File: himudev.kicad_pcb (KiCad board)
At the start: 4 copper layers, 93.6 x 43.6 mm, 132 parts, among them J1 USB_C16PIN, J2 M20-8770642R, J3 M20-8770642R, J4 20021121-00010C4LF, J5 M20-8762042, Q1 IRLML6402, Q2 BSS214NW, Q3 BSS214NW, Q4 BSS214NW, Q5 BSS214NW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

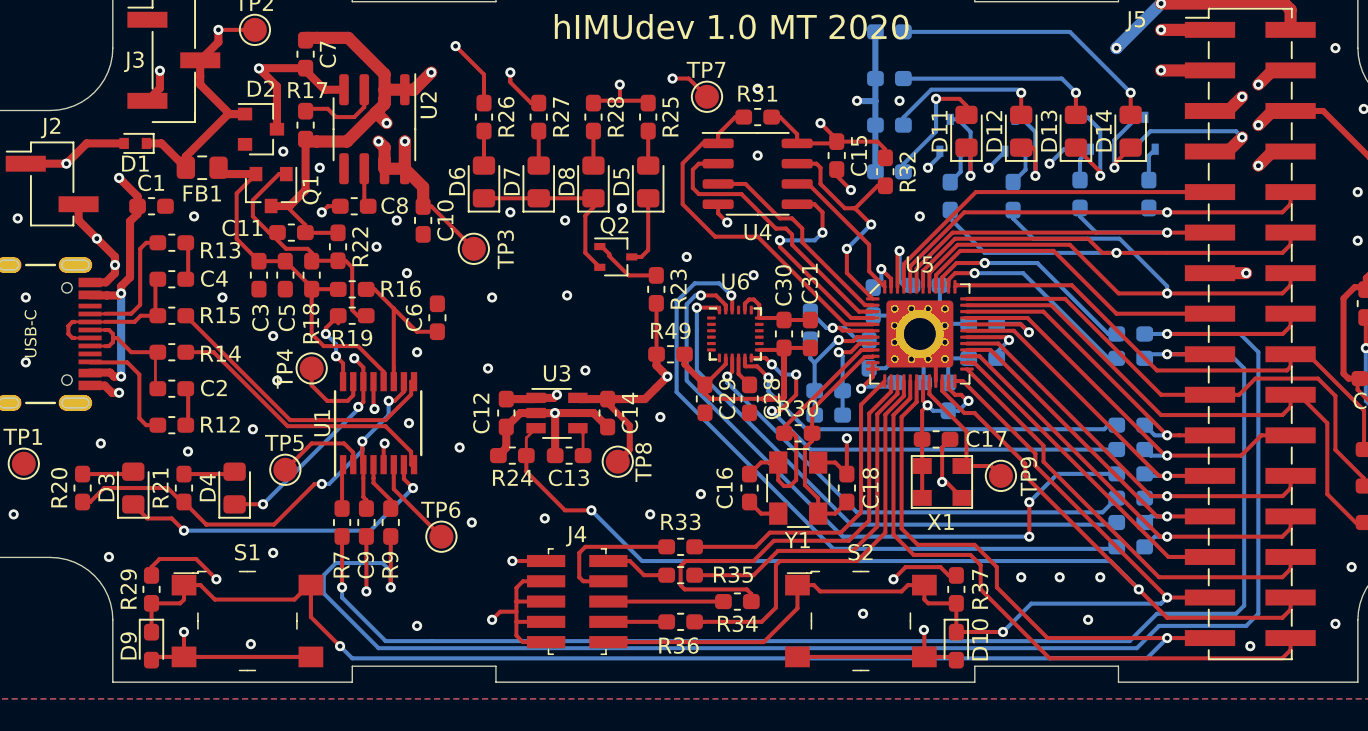
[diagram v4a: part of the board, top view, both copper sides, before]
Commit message: Small via & silkscreen fixes
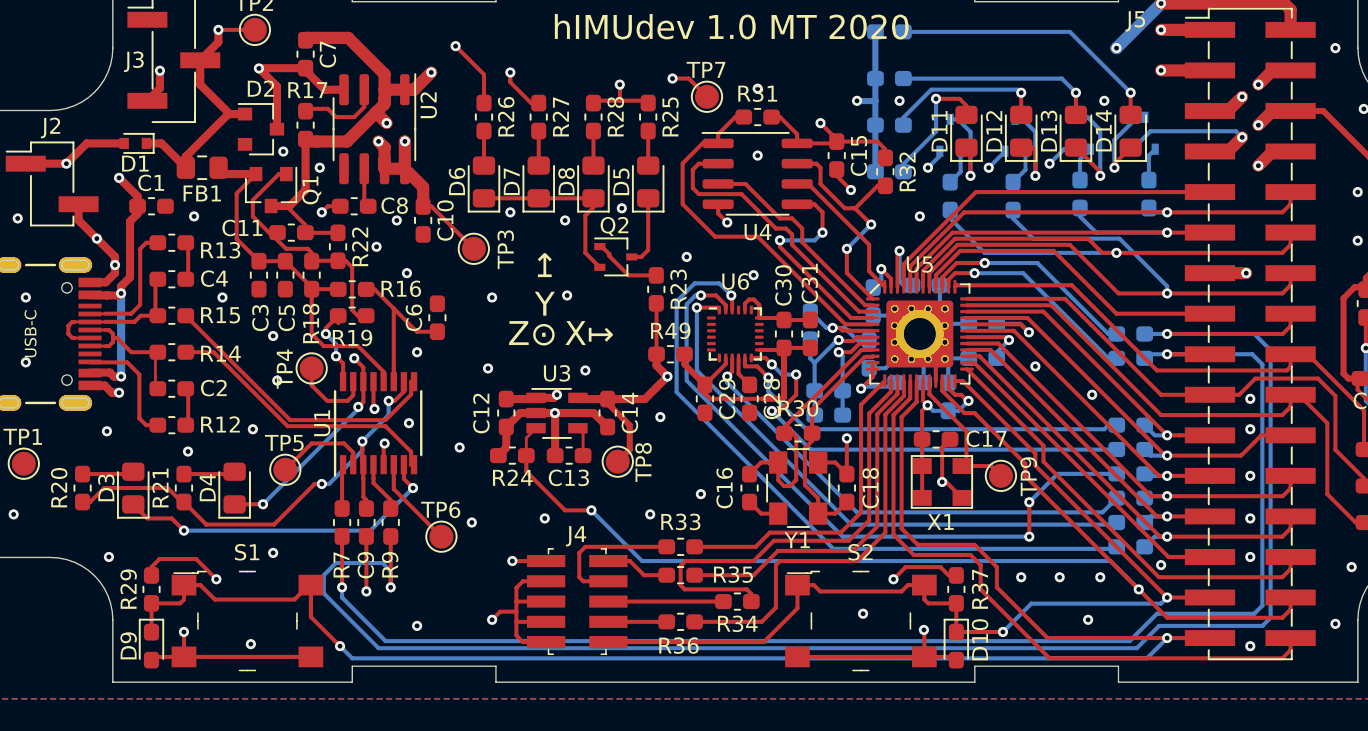
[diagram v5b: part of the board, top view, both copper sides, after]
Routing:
- net /MCU_clk_reset/CONSOLE_RX: track 86.6 -> 89.1 mm
- net /MCU_clk_reset/CONSOLE_TX: track 103.6 -> 105.4 mm
- net GND: vias 83 -> 92
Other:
- board text added: "X↦"
- board text added: "Z⊙"
- board text added: "↥ Y"

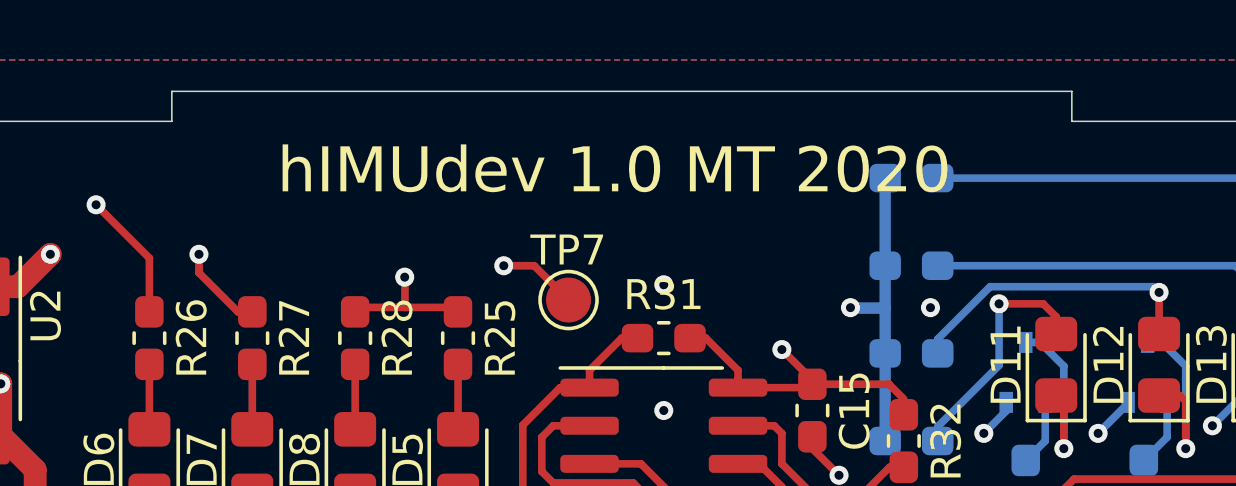
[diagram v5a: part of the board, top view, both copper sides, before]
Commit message: Add JLCPCB SN placeholder, fix silkscreen
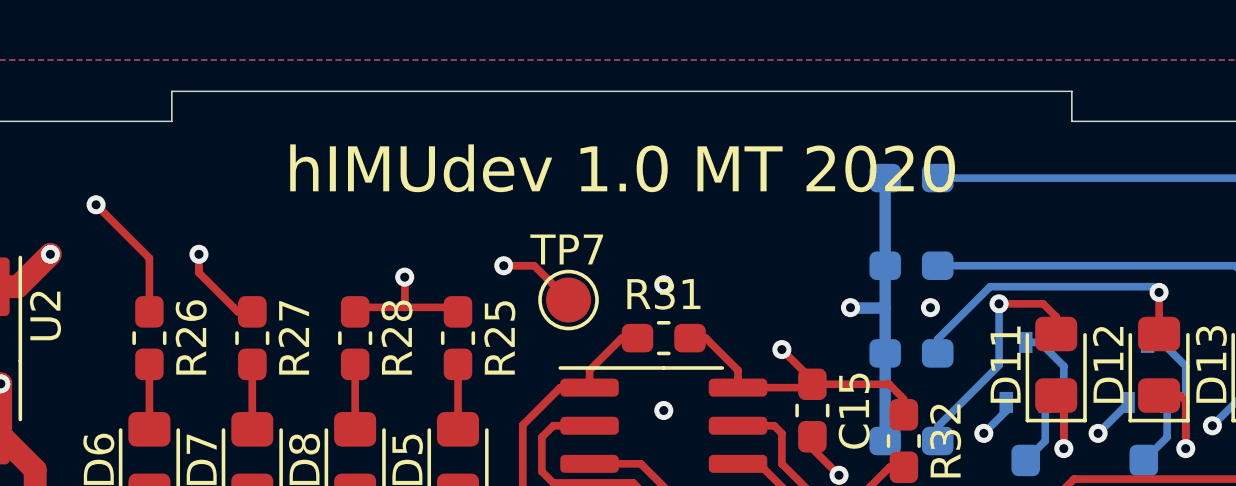
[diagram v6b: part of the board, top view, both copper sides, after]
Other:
- board text added: "JLCJLCJLCJLC"
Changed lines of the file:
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@@
   (general
     (thickness 1.6)
-    (drawings 55)
+    (drawings 49)
     (tracks 1352)
     (zones 0)
@@
     )
   )
+  (gr_text JLCJLCJLCJLC (at 152.4 81.915) (layer B.SilkS)
+    (effects (font (size 1 1) (thickness 0.15)) (justify mirror))
+  )
   (gr_text Z⊙ (at 139.7 101.6) (layer F.SilkS)
     (effects (font (size 1.5 1.5) (thickness 0.3)))
@@
     (effects (font (size 1.5 1.5) (thickness 0.3)))
   )
-  (gr_text "hIMUdev 1.0 MT 2020" (at 152.146 82.423) (layer F.SilkS)
+  (gr_text "hIMUdev 1.0 MT 2020" (at 152.4 82.423) (layer F.SilkS)
     (effects (font (size 1.5 1.5) (thickness 0.3)))
   )
@@
   (gr_line (start 176.4 80.785) (end 176.4 79.785) (layer Edge.Cuts) (width 0.05))
   (gr_line (start 167.4 80.785) (end 176.4 80.785) (layer Edge.Cuts) (width 0.05))
-  (gr_line (start 270.002 153.4666) (end 276.002 153.4666) (layer Eco1.User) (width 0.05))
   (gr_line (start 113.4 119.5075) (end 113.4 123.415) (layer Edge.Cuts) (width 0.05))
   (gr_line (start 109.4925 115.6) (end 105.585 115.6) (layer Edge.Cuts) (width 0.05))
@@
   (gr_line (start 191.4 83.6925) (end 191.4 79.785) (layer Edge.Cuts) (width 0.05))
   (gr_arc (start 195.3075 83.6925) (end 191.4 83.6925) (angle -90) (layer Edge.Cuts) (width 0.05))
-  (gr_line (start 274.402 151.498) (end 276.002 151.498) (layer Eco1.User) (width 0.05))
-  (gr_line (start 274.402 152.568) (end 274.402 151.498) (layer Eco1.User) (width 0.05))
-  (gr_line (start 270.002 152.568) (end 274.402 152.568) (layer Eco1.User) (width 0.05))
-  (gr_line (start 276.002 156.718) (end 276.002 151.498) (layer Eco1.User) (width 0.05))
-  (gr_line (start 270.002 156.718) (end 270.002 152.568) (layer Eco1.User) (width 0.05))
-  (gr_line (start 270.002 156.718) (end 276.002 156.718) (layer Eco1.User) (width 0.05))
   (gr_line (start 105.585 87.6) (end 105.585 115.6) (layer Edge.Cuts) (width 0.05))
   (gr_line (start 199.215 87.6) (end 199.215 115.6) (layer Edge.Cuts) (width 0.05))
